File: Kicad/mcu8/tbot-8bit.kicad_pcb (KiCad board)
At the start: 2 copper layers, 80 x 100 mm, 62 parts, among them IC101 TLV1117-50, IC201 PIC16F1778, IC301 MCP2221A, K101 Battery, K201 MCU 1, K202 ICSP, K203 MCU 2, K301 FRONT #1, K302 FRONT #2, K303 VIN, K304 +5V, K305 FRONT #3, K306 SERVO LEFT, K307 USB/UART, K308 SERVO RIGHT, T101 DMP2305U, T102 DMP2305U

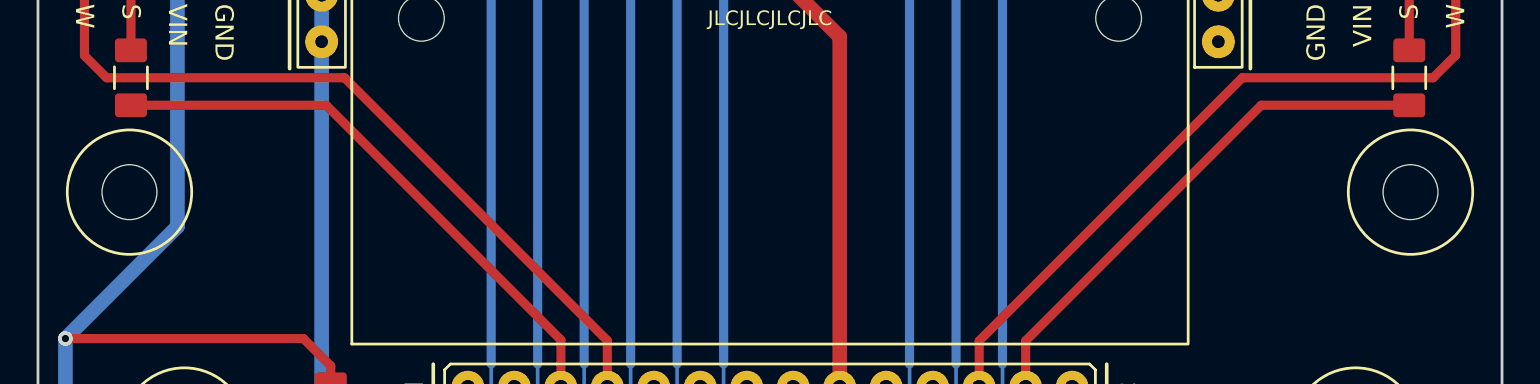
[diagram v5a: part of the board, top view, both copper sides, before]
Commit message: Update MCU 8Bit
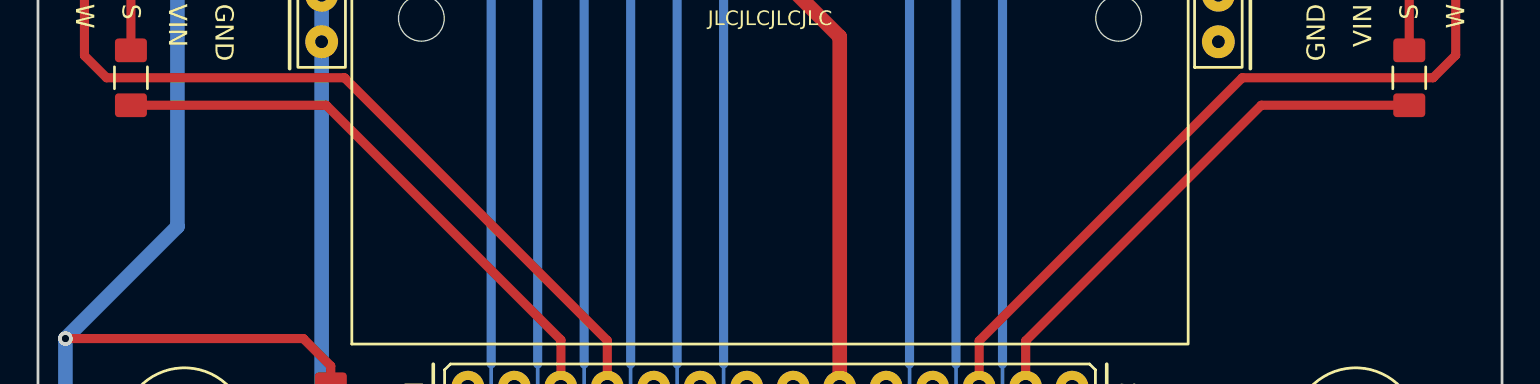
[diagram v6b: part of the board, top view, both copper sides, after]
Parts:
- removed H107, H108: MOUNTING-HOLE-3MM, tronixio:M3
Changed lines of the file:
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@@
     )
-  )
-  (footprint "tronixio:M3" (layer "F.Cu")
-    (at 175 86)
-    (property "Sheetfile" "tbot-8bit.kicad_sch")
-    (property "Sheetname" "")
-    (attr exclude_from_pos_files)
-    (fp_text reference "H107" (at 0 -4.2) (layer "F.Fab") hide
-      (effects (font (size 1 1) (thickness 0.15)))
-    )
-    (fp_text value "MOUNTING-HOLE-3MM" (at 0 4.2) (layer "F.Fab") hide
-      (effects (font (size 1 1) (thickness 0.15)))
-    )
-    (fp_circle (center 0 0) (end 3.4 0) (layer "B.SilkS") (width 0.15) (fill none))
-    (fp_circle (center 0 0) (end 3.4 0) (layer "F.SilkS") (width 0.15) (fill none))
-    (fp_circle (center 0 0) (end 3.4 0) (layer "F.CrtYd") (width 0.05) (fill none))
-    (pad "" np_thru_hole circle (at 0 0) (size 3 3) (drill 3) (layers F&B.Cu *.Mask))
   )
   (footprint "tronixio:CAPACITOR-ELECTROLYTIC-RADIAL-080-115-035" (layer "F.Cu")
@@
     )
   )
-  (footprint "tronixio:M3" (layer "F.Cu")
-    (at 105 86)
-    (property "Sheetfile" "tbot-8bit.kicad_sch")
-    (property "Sheetname" "")
-    (attr exclude_from_pos_files)
-    (fp_text reference "H108" (at 0 -4.2) (layer "F.Fab") hide
-      (effects (font (size 1 1) (thickness 0.15)))
-    )
-    (fp_text value "MOUNTING-HOLE-3MM" (at 0 4.2) (layer "F.Fab") hide
-      (effects (font (size 1 1) (thickness 0.15)))
-    )
-    (fp_circle (center 0 0) (end 3.4 0) (layer "B.SilkS") (width 0.15) (fill none))
-    (fp_circle (center 0 0) (end 3.4 0) (layer "F.SilkS") (width 0.15) (fill none))
-    (fp_circle (center 0 0) (end 3.4 0) (layer "F.CrtYd") (width 0.05) (fill none))
-    (pad "" np_thru_hole circle (at 0 0) (size 3 3) (drill 3) (layers F&B.Cu *.Mask))
-  )
   (footprint "tronixio:CAPACITOR-1206" (layer "F.Cu")

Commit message: Update tbot-8bit.kicad_pcb
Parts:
- C302: value 470n -> 100n
- C303: value 100n -> 470n
- moved C302 13.0 mm to (169.5, 136.0), turned to -90 degrees
- moved C303 13.0 mm to (156.5, 136.0), turned to 90 degrees
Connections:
- C302 pad 1: Net-(C302-Pad1) -> +5V
- C303 pad 1: VUSB -> Net-(C303-Pad1)
- IC301 pad 1: VUSB -> +5V
- IC301 pad 11: Net-(C302-Pad1) -> Net-(C303-Pad1)
- K307 pad 1: VUSB -> unconnected-(K307-Pad1)
- LED302 pad 2: VUSB -> +5V
- LED303 pad 2: VUSB -> +5V
- R306 pad 2: VUSB -> +5V
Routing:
- net +5V: track 193.7 -> 257.7 mm, vias 6 -> 9
- net VUSB: track 37.6 -> 0.00 mm, vias 3 -> 0
- net Net-(C303-Pad1): track 0.00 -> 10.0 mm
- net Net-(C302-Pad1): track 10.0 -> 0.00 mm
